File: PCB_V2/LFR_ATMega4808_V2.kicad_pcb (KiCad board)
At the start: 2 copper layers, 70.5 x 90 mm, 68 parts, among them J1 Conn_02x02_Odd_Even, J2 Conn_02x05_Odd_Even, J3 Conn_01x03, J4 Conn_01x03, J5 Conn_01x03, J6 Conn_02x03_Odd_Even, J7 Conn_02x02_Odd_Even, J8 Conn_01x03, J9 Conn_01x03, Q1 PMOS, Q2 NMOS, Q3 NMOS, Q4 NMOS, Q5 NMOS, Q6 PMOS, Q7 NMOS, Q8 NMOS, U1 ATmega4808-A, U5 MCP1700x-330xxTO

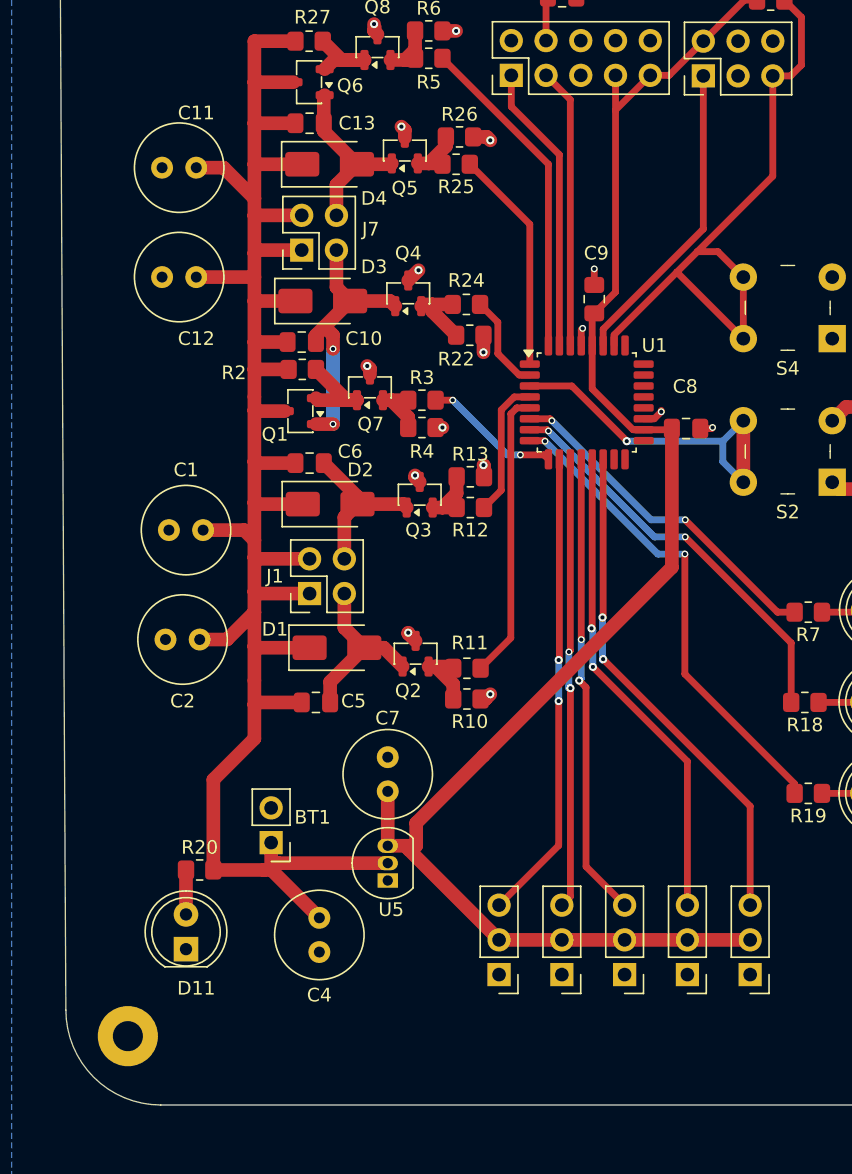
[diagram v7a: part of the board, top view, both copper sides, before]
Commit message: Added test points
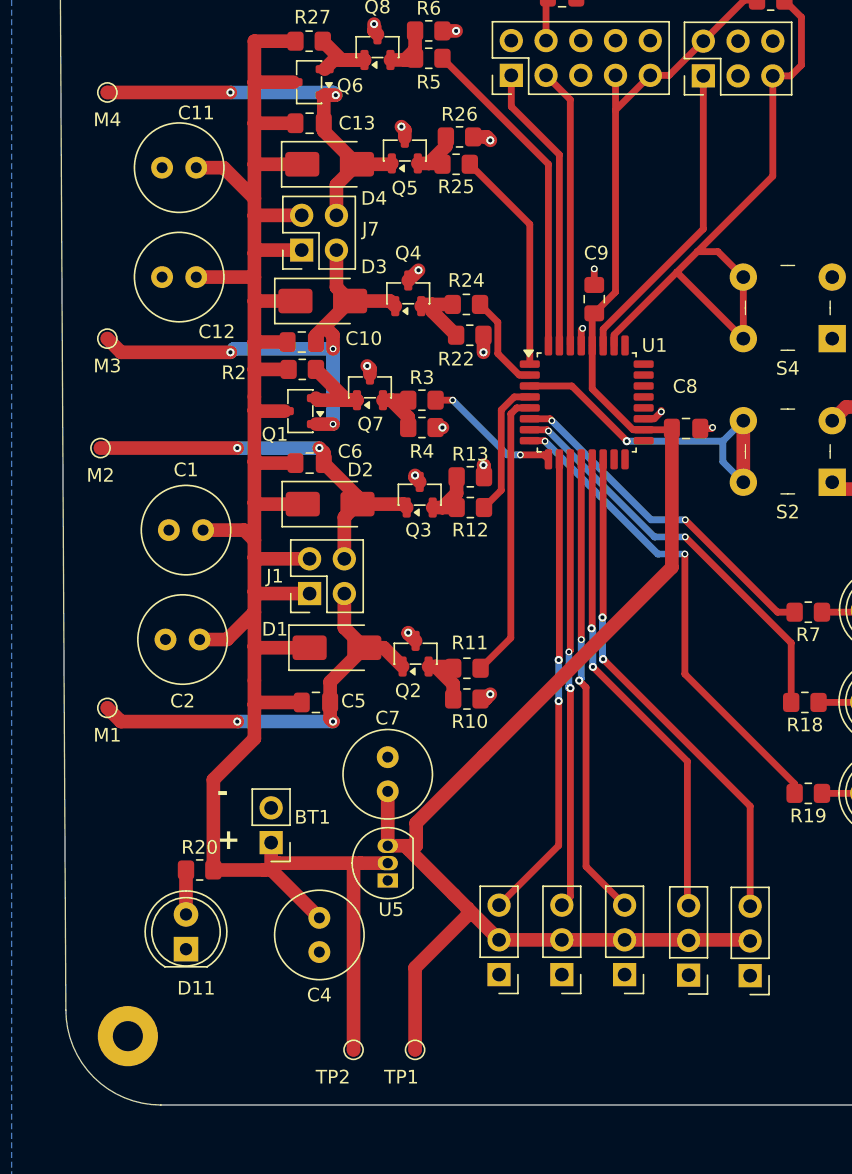
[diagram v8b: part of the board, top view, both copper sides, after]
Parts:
- removed J3, J4: Conn_01x03, Connector_PinHeader_2.54mm:PinHeader_1x03_P2.54mm_Vertical
- added J10: Conn_01x03, Connector_PinHeader_2.54mm:PinHeader_1x03_P2.54mm_Vertical, F.Cu at (159.5, 152.5)
- added J11: Conn_01x03, Connector_PinHeader_2.54mm:PinHeader_1x03_P2.54mm_Vertical, F.Cu at (164.0, 152.6)
- added M1: TestPoint, TestPoint:TestPoint_Pad_D1.0mm, F.Cu at (117.0, 133.0)
- added M2: TestPoint, TestPoint:TestPoint_Pad_D1.0mm, F.Cu at (116.5, 114.0)
- added M3: TestPoint, TestPoint:TestPoint_Pad_D1.0mm, F.Cu at (117.0, 106.0)
- added M4: TestPoint, TestPoint:TestPoint_Pad_D1.0mm, F.Cu at (117.0, 88.0)
- added TP1: TestPoint, TestPoint:TestPoint_Pad_D1.0mm, F.Cu at (139.5, 158.0)
- added TP2: TestPoint, TestPoint:TestPoint_Pad_D1.0mm, F.Cu at (135.0, 158.0)
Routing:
- net Net-(D1-A): track 13.0 -> 31.4 mm, vias 0 -> 2
- net Net-(D4-A): track 13.0 -> 30.6 mm, vias 0 -> 2
- net Net-(D2-A): track 12.1 -> 29.4 mm, vias 0 -> 2
- net Net-(D3-A): track 20.3 -> 37.3 mm, vias 2 -> 3
- net +4.8V: track 152.0 -> 165.7 mm
- net +3.3V: track 116.7 -> 128.6 mm
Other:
- board text added: "+"
- board text added: "-"
